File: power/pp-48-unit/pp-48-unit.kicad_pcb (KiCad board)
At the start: 4 copper layers, 78.5 x 72 mm, 208 parts, among them J1 NODE 19V, J2 FRONT PANEL, J201 XT60PW-M, J3 AUX, J301 CHAIN IN, J302 CHAIN OUT, J51 NODE 19V, J52 FRONT PANEL, J53 AUX, Q1 BSC070N10NS5, Q10 2N7002, Q2 2N7002, Q202 BSC040N10NS5, Q203 BSC040N10NS5, Q204 2N7002, Q3 2N7002, Q4 2N7002, Q5 2N7002, Q51 BSC070N10NS5, Q52 2N7002, Q53 2N7002, Q54 2N7002, Q55 2N7002, Q56 2N7002, Q57 2N7002, Q58 2N7002, Q59 2N7002, Q6 2N7002, Q7 2N7002, Q8 2N7002, Q9 2N7002, U1 LM5069MM-2, U10 74LVC1G74, U2 INA238AIDGSR, U207 LM5069MM-1, U208 INA238AIDGSR, U3 74LVC1G74, U4 ADC121C027CIMK, U5 TCA6424ARGJR, U51 LM5069MM-2, U52 INA238AIDGSR, U53 74LVC1G74, U54 ADC121C027CIMK, U56 TLP176AM, U57 TLP176AM, U58 TLP291, U6 TLP176AM, U60 74LVC1G74, U7 TLP176AM, U8 TLP291

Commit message: stock replacements: unit INA238 (0 at JLC) -> INA237AIDGSR C2864837 on U2 / U52 / U208 (pin- and register-compatible for the plane-logic driver: SHUNT_CAL, LSBs, DIETEMP, MANUFACTURER_ID; gain error 0.3 %); module U2 / U3 MCP65R46-1.21 (0) -> MCP65R46T-2402E/CHY C623510 (2.4 V ref, same hysteresis, open drain, pinout) with R12 84.5k / R14 61.9k (OV_KILL 22.68 V, PGOOD 17.26 V, were 22.75 / 17.30), C13 -> C2980802 (100 V, same family); LM5069-1 left open for the user; boards synced from the netlists; ERC unchanged, DRC unchanged, parity clean; handoff
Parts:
- U2, U208, U52: value INA238AIDGSR -> INA237AIDGSR
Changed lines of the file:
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@@
 			)
 		)
-		(property "Value" "INA238AIDGSR"
+		(property "Value" "INA237AIDGSR"
 			(at 0 2.45 270)
 			(layer "F.Fab")
@@
 			)
 		)
-		(property "LCSC" "C2868250"
+		(property "LCSC" "C2864837"
 			(at 0 0 270)
 			(layer "F.Fab")
@@
 			)
 		)
-		(property "MPN" "TI INA238AIDGSR"
+		(property "MPN" "TI INA237AIDGSR"
 			(at 0 0 0)
 			(layer "F.Fab")
@@
 				(font
 					(size 1.27 1.27)
+					(thickness 0.15)
 				)
 			)
@@
 			)
 		)
-		(property "Description" "INA238 VS"
+		(property "Description" "INA237 VS"
 			(at 0 0 90)
 			(layer "F.Fab")
@@
 			)
 		)
-		(property "Value" "INA238AIDGSR"
+		(property "Value" "INA237AIDGSR"
 			(at 0 2.45 270)
 			(layer "F.Fab")
@@
 			)
 		)
-		(property "LCSC" "C2868250"
+		(property "LCSC" "C2864837"
 			(at 0 0 270)
 			(layer "F.Fab")
@@
 			)
 		)
-		(property "MPN" "TI INA238AIDGSR"
+		(property "MPN" "TI INA237AIDGSR"
 			(at 0 0 0)
 			(layer "F.Fab")
@@
 				(font
 					(size 1.27 1.27)
+					(thickness 0.15)
 				)
 			)
@@
 			)
 		)
-		(property "Description" "INA238 VS"
+		(property "Description" "INA237 VS"
 			(at 0 0 90)
 			(layer "F.Fab")
@@
 			)
 		)
-		(property "Value" "INA238AIDGSR"
+		(property "Value" "INA237AIDGSR"
 			(at 0 -2.45 180)
 			(layer "B.Fab")
@@
 			)
 		)
-		(property "LCSC" "C2868250"
+		(property "LCSC" "C2864837"
 			(at 0 0 180)
 			(layer "B.Fab")
@@
 			)
 		)
-		(property "MPN" "TI INA238AIDGSR"
+		(property "MPN" "TI INA237AIDGSR"
 			(at 0 0 0)
 			(layer "B.Fab")
@@
 				(font
 					(size 1.27 1.27)
+					(thickness 0.15)
 				)
 			)
@@
 			)
 		)
-		(property "Description" "INA238 VS"
+		(property "Description" "INA237 VS"
 			(at 0 0 180)
 			(layer "B.Fab")

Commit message: pp-48-unit: unit hot-swap U207 LM5069MM-1 (latch-off, 1 at JLC) -> LM5069MM-2 C111822 (auto-retry, as the slots; user 2026-10-30); the latch moves into the core firmware: ADR 0005 decision 3 (U_PGD falling with the unit input in range -> core holds U_OFF high until unit_reset; no latch on a bus dip; no core = retry forever, unit ON), uinput.py notes, Q204 / U207 descriptions, title comment; schematic regenerated, board synced; ERC 0, DRC unchanged, parity clean; handoff
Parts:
- U207: value LM5069MM-1 -> LM5069MM-2
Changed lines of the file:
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@@
 			)
 		)
-		(property "Description" "expander U_OFF (P13) high = unit off (and resets the latched LM5069-1)"
+		(property "Description" "expander U_OFF (P13) high = unit off: the firmware latch after a unit fault"
 			(at 0 0 180)
 			(layer "B.Fab")
@@
 			)
 		)
-		(property "Value" "LM5069MM-1"
+		(property "Value" "LM5069MM-2"
 			(at 0 -2.45 180)
 			(layer "B.Fab")
@@
 			)
 		)
-		(property "Description" "unit hot-swap, 55 mV current limit, power limit, LATCH-OFF (-1); LCSC stock 1 on 2026-10-29 (LM5069MM-2 C111822 has 7k)"
+		(property "Description" "unit hot-swap, 55 mV current limit, power limit, auto-retry 0.5 % (-2); the latch is the firmware's, over U_OFF"
 			(at 0 0 180)
 			(layer "B.Fab")
@@
 			)
 		)
-		(property "LCSC" "C486026"
+		(property "LCSC" "C111822"
 			(at 0 0 180)
 			(layer "B.Fab")

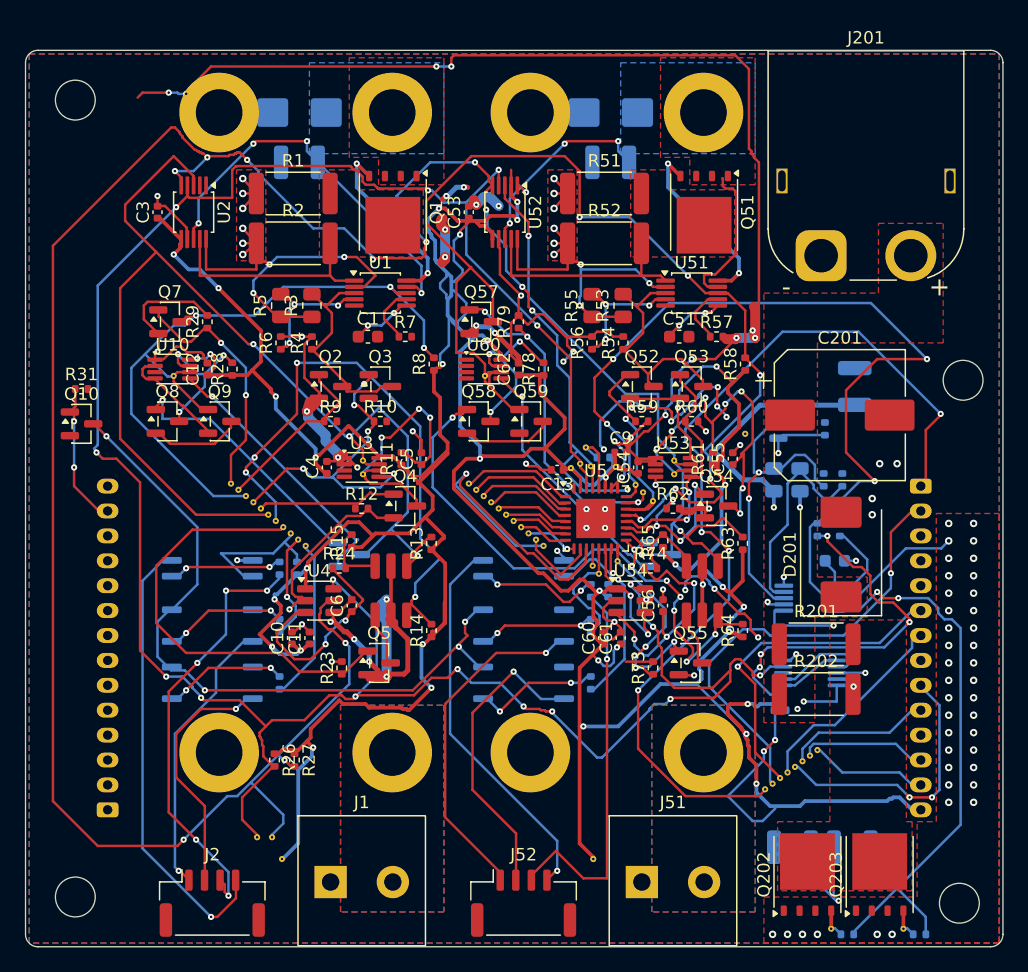
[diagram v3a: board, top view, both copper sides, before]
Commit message: pp-48-unit: pcbkit silk (refs sized / hidden on small parts, values to Fab) and prune of one dangling +3V3 stub; DRC 10 (6 known PTH-in-courtyard overrides, 3 XT60 silk at the edge, 1 starved thermal), 0 unconnected, parity clean; jlcfab runs (38 lines, 148 parts)
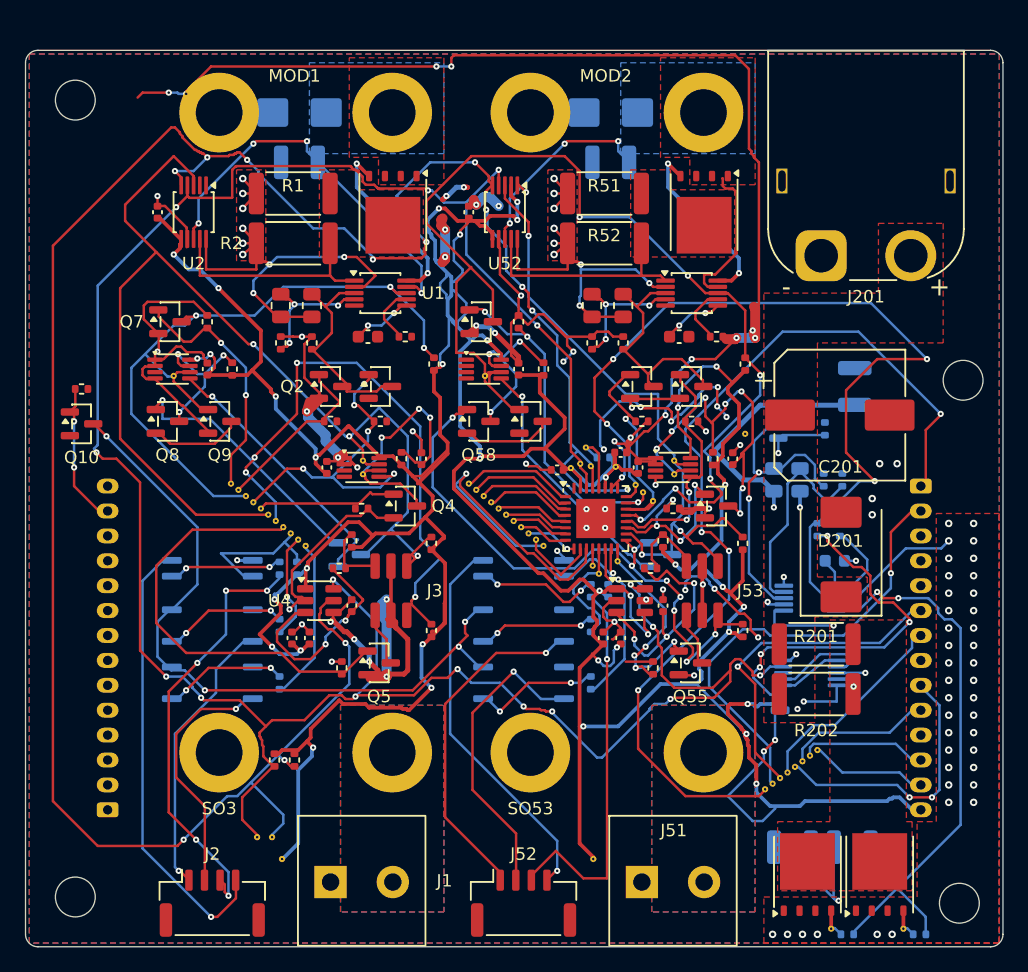
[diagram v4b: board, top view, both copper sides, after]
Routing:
- net +3V3: track 513.2 -> 512.0 mm
